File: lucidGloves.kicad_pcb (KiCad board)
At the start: 2 copper layers, 73.7 x 50.8 mm, 30 parts, among them J1 USB_C_Receptacle_PowerOnly_6P, J10 Conn_01x05_Pin, J11 Conn_01x05_Pin, J12 Conn_01x05_Pin, J13 Conn_01x19_Socket, J14 Conn_01x06_Pin, J15 Conn_01x05_Pin, J16 Conn_01x03_Pin, J17 Conn_01x03_Pin, J18 Conn_01x03_Pin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

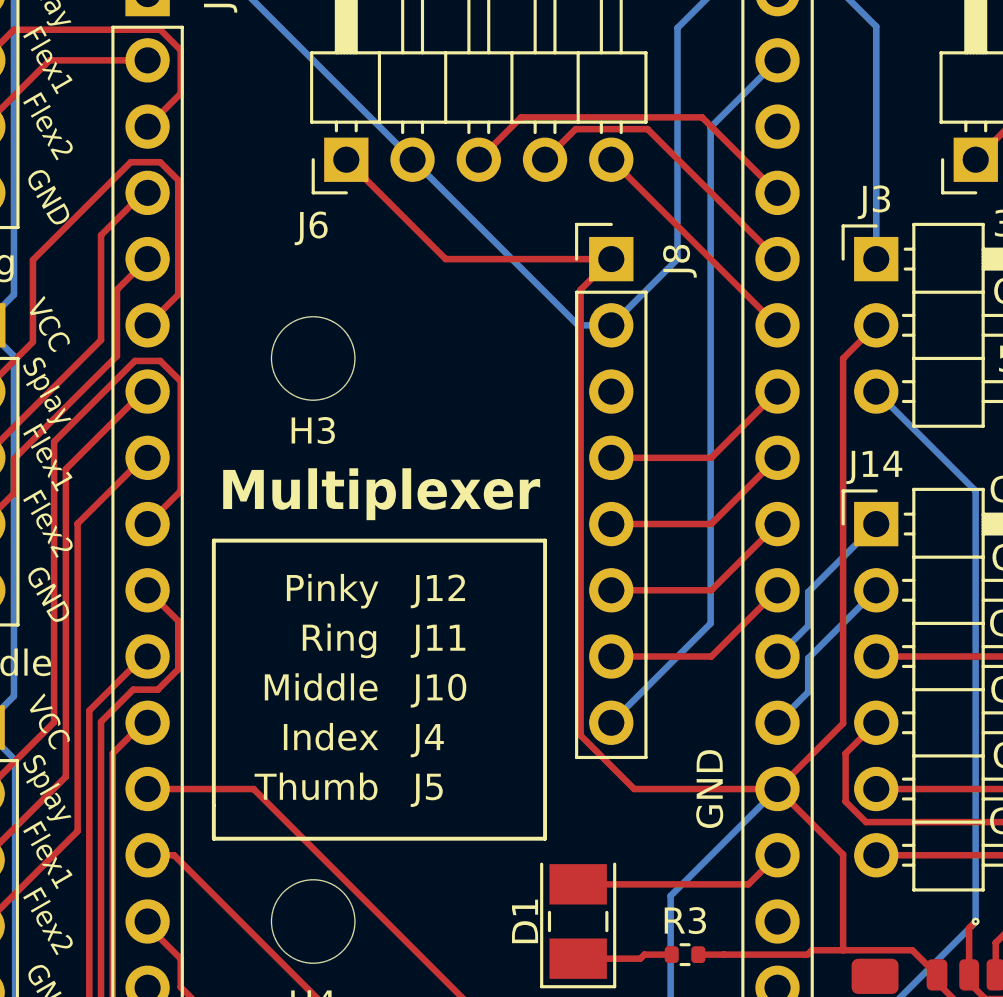
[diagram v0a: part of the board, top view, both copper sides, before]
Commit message: Fix multiplexer spacing
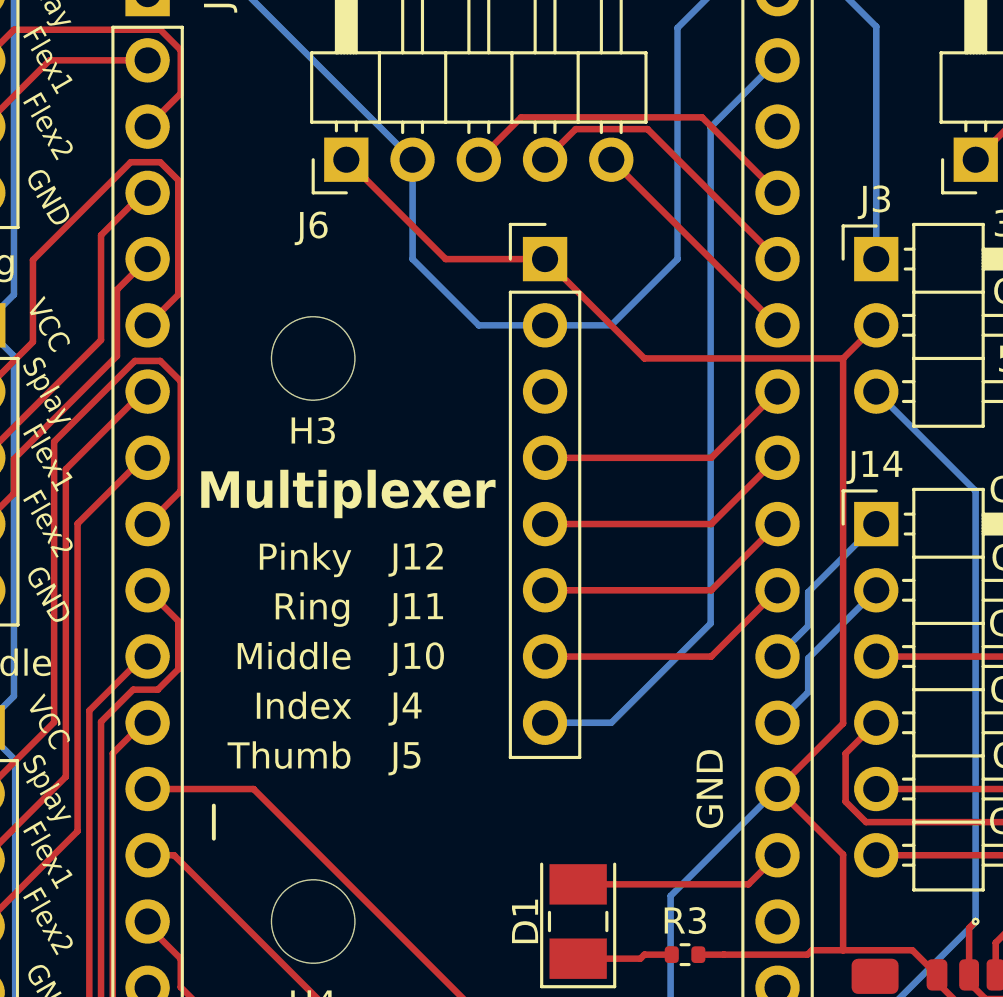
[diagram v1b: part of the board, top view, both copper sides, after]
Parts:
- moved G*** 31.8 mm to (193.0, 80.0)
- moved J8 2.54 mm to (167.6, 66.0)
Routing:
- net Net-(J10-Pin_5): track 165.8 -> 149.1 mm
- net Net-(J8-Pin_7): track 7.43 -> 9.97 mm
- net Net-(J8-Pin_5): track 7.43 -> 9.97 mm
- net Net-(J8-Pin_8): track 28.0 -> 30.6 mm
- net Net-(J8-Pin_6): track 7.43 -> 9.97 mm
- net Net-(J8-Pin_4): track 7.43 -> 9.97 mm
- net Net-(J10-Pin_1): track 134.9 -> 137.2 mm
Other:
- board text added: "https://github.com/ Glitch752/LucidGlovesPCB"
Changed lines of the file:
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@@
 		(tags "Through hole pin header THT 1x05 2.54mm single row")
 		(property "Reference" "J12"
-			(at 16.46 24.765 0)
+			(at 15.605257 23.555083 0)
 			(layer "F.SilkS")
 			(effects
@@
 		(tags "Through hole pin header THT 1x05 2.54mm single row")
 		(property "Reference" "J11"
-			(at 16.46 11.43 0)
+			(at 15.605257 10.220083 0)
 			(layer "F.SilkS")
 			(effects
@@
 		(tags "Through hole pin header THT 1x05 2.54mm single row")
 		(property "Reference" "J5"
-			(at 13.335 1.44 0)
+			(at 14.544917 0.585257 0)
 			(layer "F.SilkS")
 			(effects
@@
 		(tags "Through hole pin header THT 1x05 2.54mm single row")
 		(property "Reference" "J10"
-			(at 16.485 -2.085 180)
+			(at 15.630257 -3.294917 180)
 			(layer "F.SilkS")
 			(effects
@@
 		(tags "Through hole pin header THT 1x05 2.54mm single row")
 		(property "Reference" "J4"
-			(at 15.24 16.46 0)
+			(at 16.449917 15.605257 0)
 			(layer "F.SilkS")
 			(effects
@@
 	(footprint "Connector_PinHeader_2.54mm:PinHeader_1x08_P2.54mm_Vertical"
 		(layer "F.Cu")
-		(at 170.18 66.04)
+		(at 167.64 66.04)
 		(descr "Through hole straight pin header, 1x08, 2.54mm pitch, single row")
 		(tags "Through hole pin header THT 1x08 2.54mm single row")
@@
 			(at 2.54 0 90)
 			(layer "F.SilkS")
+			(hide yes)
 			(effects
 				(font
@@
 		(tags "resistor")
 		(property "Reference" "R3"
-			(at 0 1.27 360)
+			(at 0 1.27 0)
 			(layer "F.SilkS")
 			(effects
@@
 		)
 		(fp_text user "${REFERENCE}"
-			(at 0 0 360)
+			(at 0 0 0)
 			(layer "F.Fab")
 			(effects
@@
 	(footprint "LOGO"
 		(layer "B.Cu")
-		(at 161.29 80.01 180)
+		(at 193.04 80.01 180)
 		(property "Reference" "G***"
 			(at 0 0 0)
@@
 	)
 	(gr_line
-		(start 167.64 88.265)
-		(end 154.94 88.265)
-		(stroke
-			(width 0.15)
-			(type default)
-		)
-		(layer "F.SilkS")
-	)
-	(gr_line
 		(start 154.94 88.265)
 		(end 154.94 86.995)
@@
 	)
 	(gr_line
-		(start 167.64 76.835)
-		(end 167.64 88.265)
-		(stroke
-			(width 0.15)
-			(type default)
-		)
-		(layer "F.SilkS")
-	)
-	(gr_line
-		(start 154.94 86.995)
-		(end 154.94 76.835)
-		(stroke
-			(width 0.15)
-			(type default)
-		)
-		(layer "F.SilkS")
-	)
-	(gr_line
 		(start 150.872831 52.216257)
 		(end 149.602831 52.216257)
@@
 	)
 	(gr_line
-		(start 154.94 76.835)
-		(end 167.64 76.835)
-		(stroke
-			(width 0.15)
-			(type default)
-		)
-		(layer "F.SilkS")
-	)
-	(gr_line
 		(start 150.068416 52.630652)
 		(end 149.602831 52.216257)
@@
 	)
 	(gr_line
-		(start 170.18 85.15)
+		(start 167.64 85.09)
 		(end 152.4 85.15)
 		(stroke
@@
 	)
 	(gr_text "*"
-		(at 156.21 76.2 0)
+		(at 187.96 74.93 0)
 		(layer "B.SilkS")
 		(effects
@@
 		)
 	)
+	(gr_text "https://github.com/\nGlitch752/LucidGlovesPCB"
+		(at 189.23 57.15 0)
+		(layer "B.SilkS")
+		(effects
+			(font
+				(size 1 1)
+				(thickness 0.15)
+			)
+			(justify top mirror)
+		)
+	)
 	(gr_text "VCC"
 		(at 210.82 85.09 270)
@@
 	)
 	(gr_text "https://github.com/\nLucidVR/lucidgloves"
-		(at 189.23 54.61 0)
+		(at 189.383516 52.94923 0)
 		(layer "B.SilkS")
 		(effects
@@
 	)
 	(gr_text "Ring"
-		(at 161.29 80.01 0)
+		(at 160.253067 78.808806 0)
 		(layer "F.SilkS")
 		(effects
@@
 	)
 	(gr_text "Index"
-		(at 161.29 83.82 0)
+		(at 160.253067 82.618806 0)
 		(layer "F.SilkS")
 		(effects
@@
 	)
 	(gr_text "Thumb"
-		(at 161.29 85.725 0)
+		(at 160.253067 84.523806 0)
 		(layer "F.SilkS")
 		(effects
@@
 	)
 	(gr_text "Pinky"
-		(at 161.29 78.105 0)
+		(at 160.253067 76.903806 0)
 		(layer "F.SilkS")
 		(effects
@@
 	)
 	(gr_text "Multiplexer"
-		(at 161.29 74.93 0)
+		(at 160.02 74.93 0)
 		(layer "F.SilkS")
 		(effects
 			(font
-				(size 1.5 1.4)
+				(size 1.4 1.3)
 				(thickness 0.28)
 				(bold yes)
@@
 	)
 	(gr_text "Middle"
-		(at 161.29 81.915 0)
+		(at 160.253067 80.713806 0)
 		(layer "F.SilkS")
 		(effects
@@
 			(extension_offset 0.5) keep_text_aligned)
 	)
-	(dimension
-		(type aligned)
-		(layer "Dwgs.User")
-		(pts
-			(xy 170.18 66.04) (xy 152.4 66.04)
-		)
-		(height 0)
-		(gr_text "17.7800 mm"
-			(at 161.29 66.04 0)
-			(layer "Dwgs.User")
-			(effects
-				(font
-					(size 1 1)
-					(thickness 0.15)
-				)
-			)
-		)
-		(format
-			(prefix "")
-			(suffix "")
-			(units 3)
-			(units_format 1)
-			(precision 4)
-		)
-		(style
-			(thickness 0.15)
-			(arrow_length 1.27)
-			(text_position_mode 2)
-			(extension_height 0.58642)
-			(extension_offset 0.5) keep_text_aligned)
-	)
 	(segment
 		(start 175.44 90.015)
@@
 	)
 	(segment
-		(start 146.1 53.34)
-		(end 147.275 54.515)
+		(start 162.56 62.23)
+		(end 162.56 66.04)
 		(width 0.25)
 		(layer "B.Cu")
@@
 	(segment
 		(start 170.18 68.58)
-		(end 172.72 66.04)
+		(end 167.64 68.58)
+		(width 0.25)
+		(layer "B.Cu")
+		(net 11)
+	)
+	(segment
+		(start 146.1 53.34)
+		(end 147.275 54.515)
 		(width 0.25)
 		(layer "B.Cu")
@@
 	)
 	(segment
-		(start 170.18 68.58)
-		(end 168.91 68.58)
+		(start 172.72 66.04)
+		(end 170.18 68.58)
 		(width 0.25)
 		(layer "B.Cu")
@@
 	)
 	(segment
+		(start 162.56 66.04)
+		(end 165.1 68.58)
+		(width 0.25)
+		(layer "B.Cu")
+		(net 11)
+	)
+	(segment
 		(start 156.26 99.06)
 		(end 157.435 97.885)
@@
 	)
 	(segment
-		(start 168.91 68.58)
-		(end 162.56 62.23)
+		(start 165.1 68.58)
+		(end 167.64 68.58)
 		(width 0.25)
 		(layer "B.Cu")
@@
 	)
 	(segment
-		(start 169.005 84.306701)
-		(end 169.005 67.215)
+		(start 163.83 66.04)
+		(end 167.64 66.04)
 		(width 0.25)
 		(layer "F.Cu")
@@
 	)
 	(segment
-		(start 160.02 62.23)
-		(end 163.83 66.04)
-		(width 0.25)
-		(layer "F.Cu")
-		(net 26)
-	)
-	(segment
-		(start 169.005 67.215)
-		(end 170.18 66.04)
-		(width 0.25)
-		(layer "F.Cu")
-		(net 26)
-	)
-	(segment
 		(start 188.17 93.4875)
 		(end 188.17 94.0875)
@@
 	)
 	(segment
-		(start 183.7625 94.8625)
-		(end 182.67 93.77)
+		(start 167.64 66.04)
+		(end 171.45 69.85)
 		(width 0.25)
 		(layer "F.Cu")
@@
 	)
 	(segment
-		(start 170.18 66.04)
-		(end 163.83 66.04)
+		(start 183.7625 94.8625)
+		(end 182.67 93.77)
 		(width 0.25)
 		(layer "F.Cu")
@@
 	)
 	(segment
-		(start 171.058299 86.36)
-		(end 169.005 84.306701)
+		(start 160.02 62.23)
+		(end 163.83 66.04)
 		(width 0.25)
 		(layer "F.Cu")
@@
 	)
 	(segment
-		(start 176.555 86.36)
-		(end 171.058299 86.36)
+		(start 171.45 69.85)
+		(end 179.07 69.85)
 		(width 0.25)
 		(layer "F.Cu")
@@
 	)
 	(segment
-		(start 174.015 76.2)
-		(end 176.555 73.66)
+		(start 176.555 73.66)
+		(end 174.015 76.2)
 		(width 0.25)
 		(layer "F.Cu")
@@
 	)
 	(segment
-		(start 170.18 76.2)
-		(end 174.015 76.2)
+		(start 174.015 76.2)
+		(end 167.64 76.2)
 		(width 0.25)
 		(layer "F.Cu")
@@
 	)
 	(segment
-		(start 170.18 78.74)
+		(start 176.555 76.2)
 		(end 174.015 78.74)
 		(width 0.25)
@@
 	(segment
 		(start 174.015 78.74)
-		(end 176.555 76.2)
+		(end 167.64 78.74)
 		(width 0.25)
 		(layer "F.Cu")
@@
 	)
 	(segment
-		(start 170.18 81.28)
+		(start 176.555 78.74)
 		(end 174.015 81.28)
 		(width 0.25)
@@
 	(segment
 		(start 174.015 81.28)
-		(end 176.555 78.74)
+		(end 167.64 81.28)
 		(width 0.25)
 		(layer "F.Cu")
@@
 	)
 	(segment
-		(start 170.18 73.66)
-		(end 174.015 73.66)
+		(start 174.015 73.66)
+		(end 167.64 73.66)
 		(width 0.25)
 		(layer "F.Cu")
@@
 	)
 	(segment
-		(start 174.015 73.66)
-		(end 176.555 71.12)
+		(start 176.555 71.12)
+		(end 174.015 73.66)
 		(width 0.25)
 		(layer "F.Cu")
@@
 		(width 0.25)
 		(layer "B.Cu")
+		(net 44)
+	)
+	(segment
+		(start 170.18 83.82)
+		(end 167.64 83.82)
+		(width 0.25)
+		(layer "B.Cu")
